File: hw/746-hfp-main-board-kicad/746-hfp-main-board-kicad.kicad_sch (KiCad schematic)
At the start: 44 parts, among them J1 5V, J10 Conn_01x01_Socket, J11 Conn_01x01_Socket, J12 Phone_Connector, J13 ESP32_Left_Pins, J14 ESP32_Right_Pins, J15 Power_Connector, J17 Control_board_connector, J18 Conn_01x01_Socket, J2 GND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

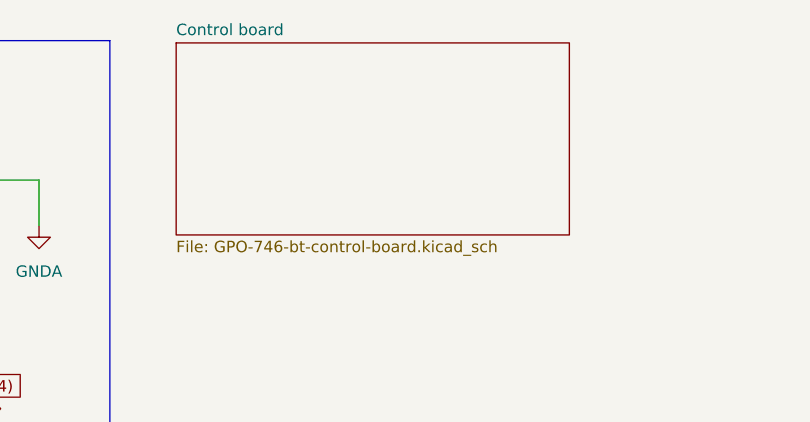
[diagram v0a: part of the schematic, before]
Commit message: Add schematic & pcb for control board
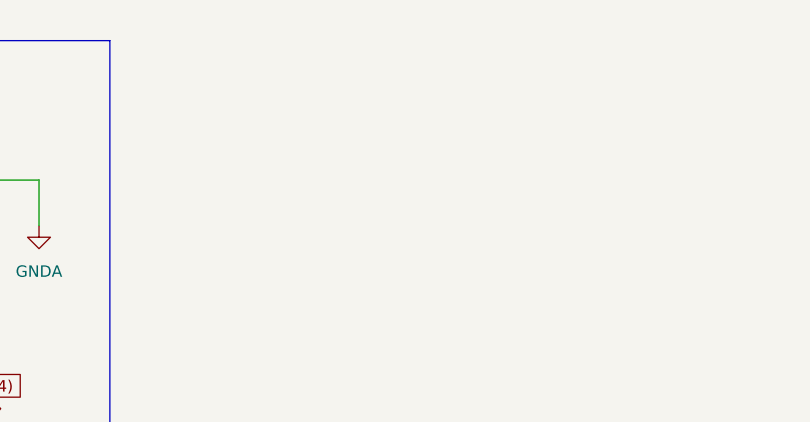
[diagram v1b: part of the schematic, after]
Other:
- removed sheet Control board

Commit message: Create kicad pcb
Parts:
- C6: value 2.2nF -> 3.3nF
- J15: footprint Connector_PinHeader_2.54mm:PinHeader_1x02_P2.54mm_Vertical -> Connector_JST:JST_XH_B2B-XH-A_1x02_P2.50mm_Vertical
- R3: value 20k -> 10k
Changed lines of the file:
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@@
   (symbol (lib_id "Device:C") (at 487.68 280.416 180) (unit 1)
     (in_bom yes) (on_board yes) (dnp no) (fields_autoplaced)
-    (property "Reference" "C6" (at 491.5408 279.146 0)
+    (property "Reference" "C6" (at 491.49 279.146 0)
       (effects (font (size 1.27 1.27)) (justify right))
     )
-    (property "Value" "2.2nF" (at 491.5408 281.686 0)
+    (property "Value" "3.3nF" (at 491.49 281.686 0)
       (effects (font (size 1.27 1.27)) (justify right))
     )
@@
       (effects (font (size 1.27 1.27)) (justify left))
     )
-    (property "Footprint" "Connector_PinHeader_2.54mm:PinHeader_1x02_P2.54mm_Vertical" (at 39.37 217.17 0)
+    (property "Footprint" "Connector_JST:JST_XH_B2B-XH-A_1x02_P2.50mm_Vertical" (at 39.37 217.17 0)
       (effects (font (size 1.27 1.27)) hide)
     )
@@
       (effects (font (size 1.27 1.27)))
     )
-    (property "Value" "20k" (at 481.33 268.8844 90)
-      (effects (font (size 1.27 1.27)))
-    )
+    (property "Value" "10k" (at 481.33 268.8844 90)
+      (effects (font (size 1.27 1.27)))
+    )

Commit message: Fixed pcb
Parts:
- Q1: footprint Package_TO_SOT_THT:TO-220-3_Vertical -> Package_TO_SOT_THT:TO-92
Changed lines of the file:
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@@
   (symbol (lib_id "Simulation_SPICE:NMOS") (at 187.96 71.12 0) (unit 1)
     (in_bom yes) (on_board yes) (dnp no) (fields_autoplaced)
-    (property "Reference" "Q1" (at 193.548 69.85 0)
+    (property "Reference" "Q1" (at 194.31 69.85 0)
       (effects (font (size 1.27 1.27)) (justify left))
     )
-    (property "Value" "IRFZ44N" (at 193.548 72.39 0)
+    (property "Value" "IRFZ44N" (at 194.31 72.39 0)
       (effects (font (size 1.27 1.27)) (justify left))
     )
-    (property "Footprint" "Package_TO_SOT_THT:TO-220-3_Vertical" (at 193.04 68.58 0)
+    (property "Footprint" "Package_TO_SOT_THT:TO-92" (at 193.04 68.58 0)
       (effects (font (size 1.27 1.27)) hide)
     )

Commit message: Fixed board
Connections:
- net Audio_SCL (27): now also J13.10 (Pin_10); no longer J13.8 (Pin_8)
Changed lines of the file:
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@@
   (junction (at 383.54 226.06) (diameter 0) (color 0 0 0 0)
   )
-  (junction (at 116.84 218.44) (diameter 0) (color 0 0 0 0)
-  )
   (junction (at 408.94 269.24) (diameter 0) (color 0 0 0 0)
   )
@@
   (junction (at 386.08 241.3) (diameter 0) (color 0 0 0 0)
   )
+  (junction (at 116.84 223.52) (diameter 0) (color 0 0 0 0)
+  )
   (junction (at 375.92 205.74) (diameter 0) (color 0 0 0 0)
   )
@@
     (stroke (width 0) (type default))
   )
-  (wire (pts (xy 116.84 218.44) (xy 116.84 271.78))
+  (wire (pts (xy 116.84 218.44) (xy 116.84 223.52))
     (stroke (width 0) (type default))
   )
@@
     (stroke (width 0) (type default))
   )
+  (wire (pts (xy 116.84 223.52) (xy 139.7 223.52))
+    (stroke (width 0) (type default))
+  )
   (wire (pts (xy 167.64 215.9) (xy 215.9 215.9))
     (stroke (width 0) (type default))
@@
     (stroke (width 0) (type default))
   )
-  (wire (pts (xy 116.84 218.44) (xy 139.7 218.44))
-    (stroke (width 0) (type default))
-  )
   (wire (pts (xy 370.84 203.2) (xy 365.76 203.2))
     (stroke (width 0) (type default))
@@
     (stroke (width 0) (type default))
   )
+  (wire (pts (xy 116.84 223.52) (xy 116.84 271.78))
+    (stroke (width 0) (type default))
+  )

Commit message: Added BOM
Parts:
- Q1: value IRFZ44N -> 2N7000
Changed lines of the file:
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@@
       (effects (font (size 1.27 1.27)) (justify left))
     )
-    (property "Value" "IRFZ44N" (at 194.31 72.39 0)
+    (property "Value" "2N7000" (at 194.31 72.39 0)
       (effects (font (size 1.27 1.27)) (justify left))
     )
